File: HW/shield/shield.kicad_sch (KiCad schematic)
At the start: 28 parts

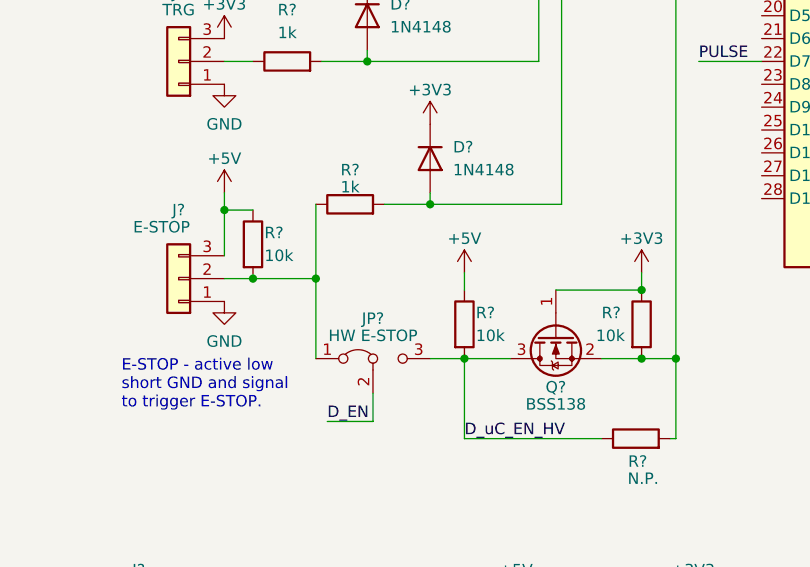
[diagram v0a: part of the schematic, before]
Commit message: added note about e-stop
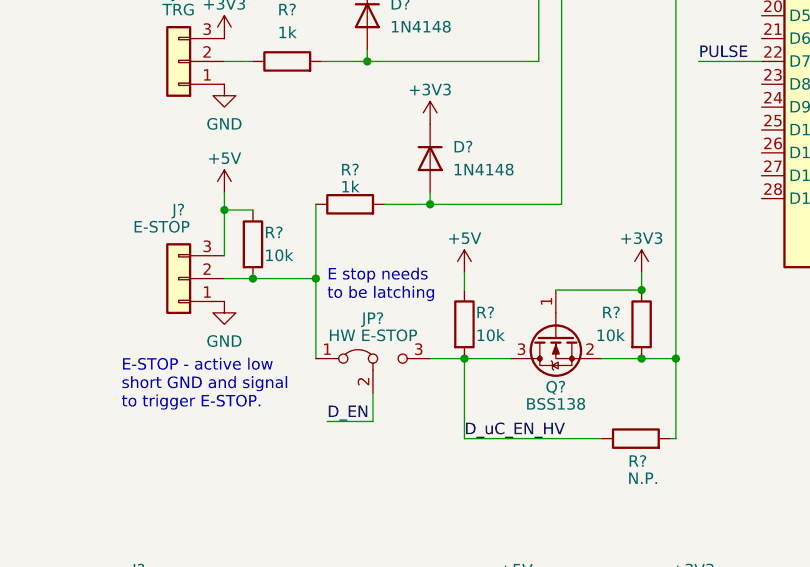
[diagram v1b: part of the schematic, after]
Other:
- note added: "E stop needs to be latching"
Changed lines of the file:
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@@
+    (effects (font (size 1.27 1.27)) (justify left bottom))
+  )
+  (text "E stop needs\nto be latching" (at 80.01 126.365 0)
     (effects (font (size 1.27 1.27)) (justify left bottom))
   )

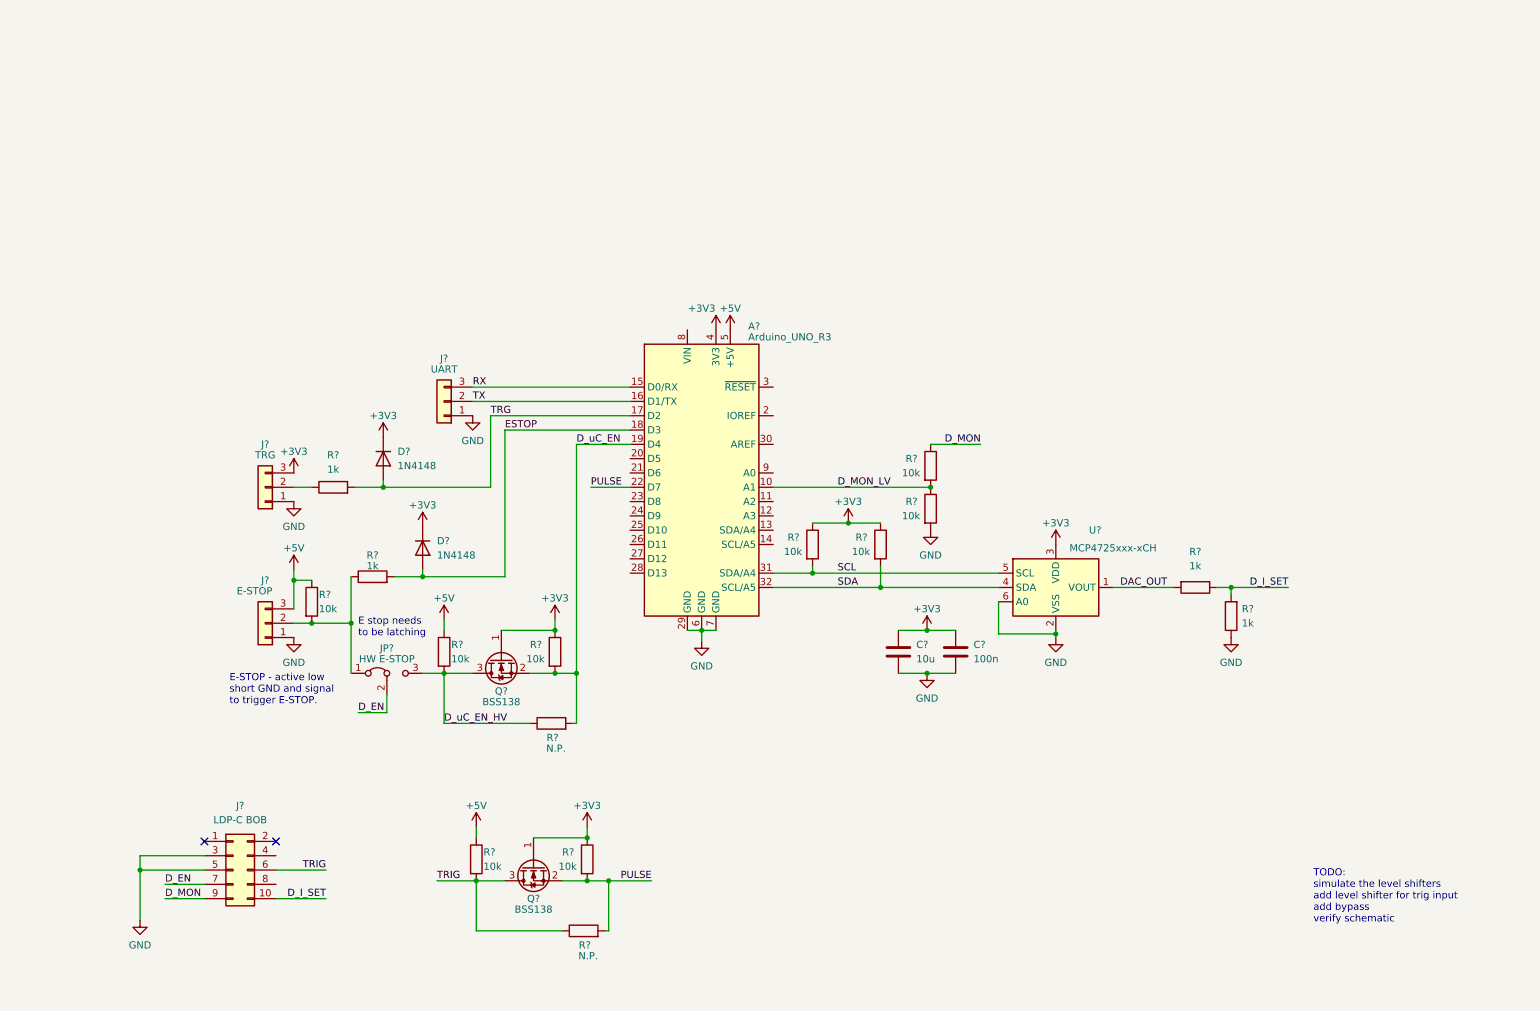
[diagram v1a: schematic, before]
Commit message: added simulation and started woking on photodiode amp
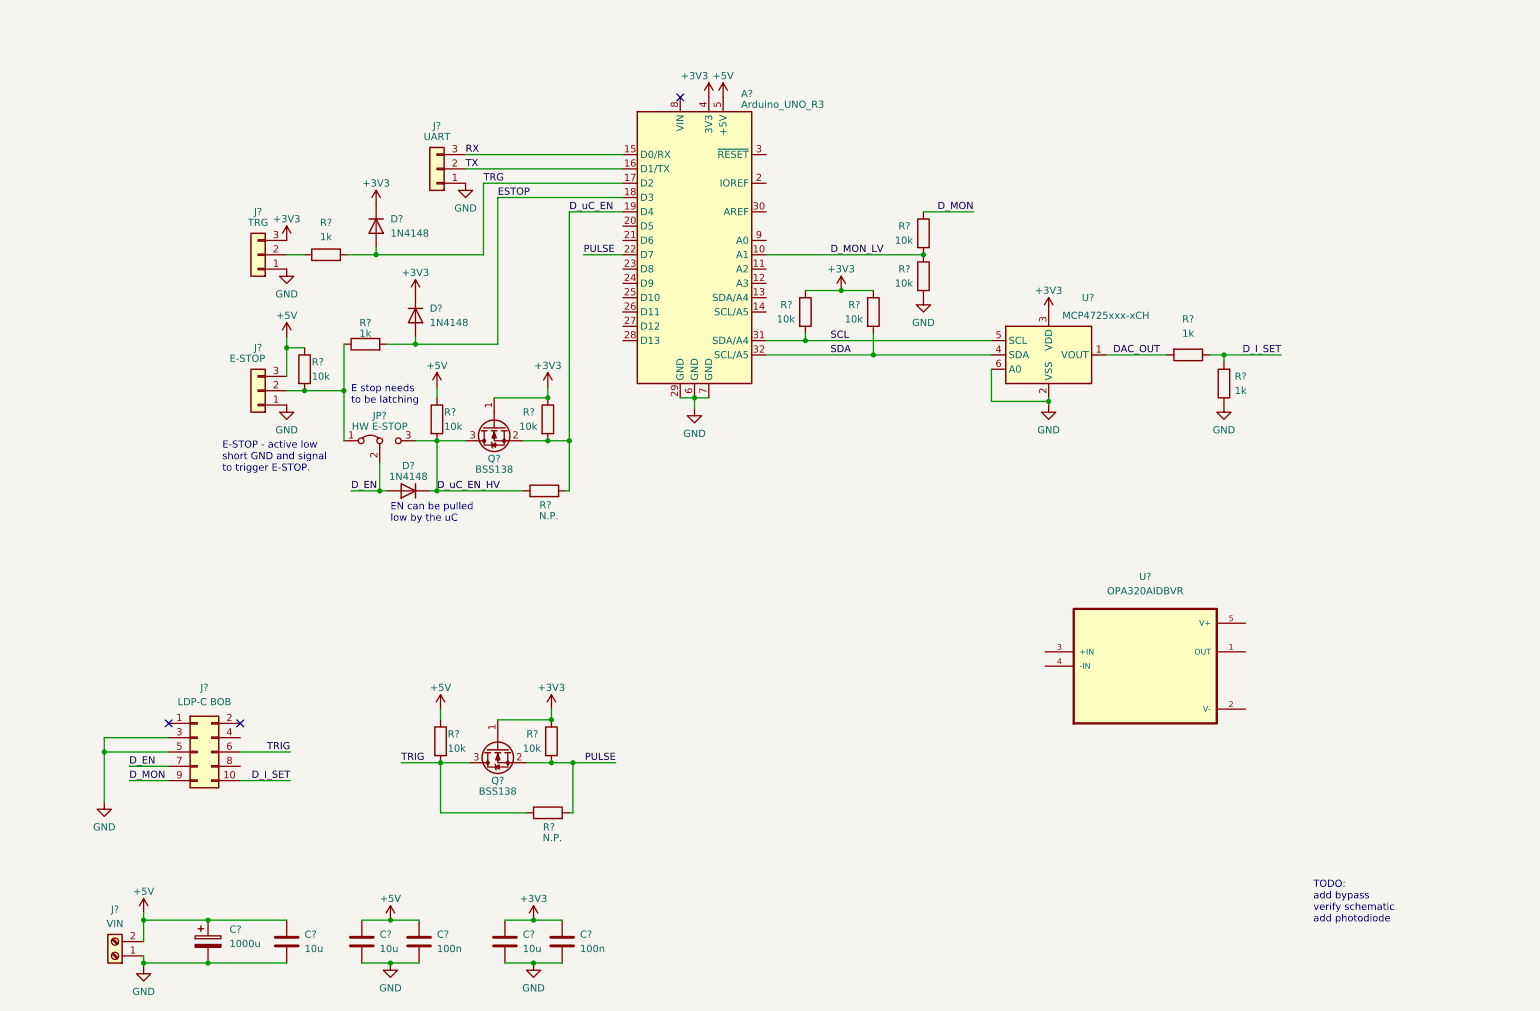
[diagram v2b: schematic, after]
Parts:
- added C?: 100n, symbol Device:C
- added C? (x2): 10u, symbol Device:C
- added C?: 1000u, symbol Device:C_Polarized
- added D?: 1N4148, symbol Device:D
- added J?: VIN, symbol Connector:Screw_Terminal_01x02
- added U?: OPA320AIDBVR, SOT95P280X145-5N, symbol OPA320AIDBVR:OPA320AIDBVR
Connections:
- net +5V: now also C?.1, C?.1, C?.1, C?.1, J?.2 (Pin_2)
- net D_EN: now also D?.2 (A)
- net D_uC_EN_HV: now also D?.1 (K)
- net GND: now also C?.2, C?.2, C?.2, C?.2, J?.1 (Pin_1)
- no-connect marks 2 -> 3
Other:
- note added: "EN can be pulled low by the uC"
- note added: "TODO: add bypass verify schematic add photodiode"
- note removed: "TODO: simulate the level shifters add level shifter for trig input add bypass verify schematic"
- moved on the sheet: A?, C?, D?, J?, JP?, Q?, R?, U?

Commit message: finished schematic
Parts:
- removed U?: OPA320AIDBVR, SOT95P280X145-5N, symbol OPA320AIDBVR:OPA320AIDBVR
- added C?: 10p, symbol Device:C
- added C? (x2): 100n, symbol Device:C
- added C?: 10u, symbol Device:C
- added D?: SFH 213, symbol Device:D_Photo
- added H? (x2): MountingHole, symbol Mechanical:MountingHole
- added J?: BREAK, symbol Connector_Generic:Conn_02x03_Odd_Even
- added J?: IO, symbol Connector:Screw_Terminal_01x06
- added Q? (x4): BSS138, Package_TO_SOT_SMD:SOT-23, symbol Transistor_FET:BSS138
- added R? (x4): N.P., symbol Device:R
- added R? (x12): 10k, symbol Device:R
- added R? (x2): 100, symbol Device:R
- added R?: 50, symbol Device:R
- added U? (x3): MCP6477-E, Package_SO:MSOP-8_3x3mm_P0.65mm, symbol Amplifier_Operational:MCP6L02x-xMS
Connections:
- net +3V3: now also Q?.1 (G), Q?.1 (G), Q?.1 (G), Q?.1 (G), R?.1, R?.1, R?.1, R?.1
- net +5V: now also C?.1, C?.1, J?.1 (Pin_1), J?.2 (Pin_2), J?.6 (Pin_6), R?.1, R?.1, R?.1, R?.1, R?.2, U?.8 (V+)
- net GND: now also C?.1, C?.2, C?.2, D?.2 (A), J?.1 (Pin_1), J?.5 (Pin_5), J?.6 (Pin_6), R?.2, U?.4 (V-), U?.5 (+)
- net IO1: now reaches A?.23 (D8)
- net IO1: now also Q?.2 (S), R?.2, R?.2
- net IO2: now reaches A?.24 (D9)
- net IO2: now also Q?.2 (S), R?.2, R?.2
- net IO3: now reaches A?.25 (D10)
- net IO3: now also Q?.2 (S), R?.2, R?.2
- net IO4: now reaches A?.26 (D11)
- net IO4: now also Q?.2 (S), R?.2, R?.2
- net D_VOUT: now reaches A?.9 (A0)
- net D_VOUT: now also J?.3 (Pin_3), J?.4 (Pin_4), R?.1
- new net: C?.1, D?.1 (K), R?.2, U?.2 (-)
- new net: C?.2, R?.1, R?.2, U?.1
- new net: R?.1, R?.2 (x3)
- new net: U?.6 (-), U?.7
- new net GUARD: C?.2, R?.1, R?.1, U?.3 (+)
- new net HV_IO1: J?.5 (Pin_5), Q?.3 (D), R?.1, R?.2
- new net HV_IO2: J?.4 (Pin_4), Q?.3 (D), R?.1, R?.2
- new net HV_IO3: J?.3 (Pin_3), Q?.3 (D), R?.1, R?.2
- new net HV_IO4: J?.2 (Pin_2), Q?.3 (D), R?.1, R?.2
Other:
- note added: "N.P."
- note added: "https://www.ti.com/lit/ug/tidu535/tidu535.pdf"
- moved on the sheet: A?, C?, D?, J?, JP?, Q?, R?, U?

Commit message: changed op amp added simulation of photodiode
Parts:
- U? (x3): value MCP6477-E -> OPA2727
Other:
- note added: "TODO: verify schematic"
- note removed: "TODO: add bypass verify schematic add photodiode"
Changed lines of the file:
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@@
     (stroke (width 0) (type default) (color 0 0 0 0))
   )
-  (text "TODO:\nadd bypass\nverify schematic\nadd photodiode" (at 249.555 177.165 0)
+  (text "TODO:\nverify schematic" (at 249.555 177.165 0)
     (effects (font (size 1.27 1.27)) (justify left bottom))
   )
@@
   (symbol (lib_id "Amplifier_Operational:MCP6L02x-xMS") (at 176.53 132.715 0) (unit 1)
     (in_bom yes) (on_board yes) (fields_autoplaced)
-    (property "Reference" "U?" (id 0) (at 176.53 122.555 0))
-    (property "Value" "MCP6477-E" (id 1) (at 176.53 125.095 0))
+    (property "Reference" "U?" (id 0) (at 176.53 121.92 0))
+    (property "Value" "OPA2727" (id 1) (at 176.53 124.46 0))
     (property "Footprint" "Package_SO:MSOP-8_3x3mm_P0.65mm" (id 2) (at 179.07 132.715 0)
       (effects (font (size 1.27 1.27)) hide)
@@
   )
   (symbol (lib_id "Connector_Generic:Conn_02x03_Odd_Even") (at 226.695 132.715 0) (unit 1)
-    (in_bom yes) (on_board yes) (fields_autoplaced)
-    (property "Reference" "J?" (id 0) (at 227.965 123.825 0))
-    (property "Value" "BREAK" (id 1) (at 227.965 126.365 0))
+    (in_bom yes) (on_board yes)
+    (property "Reference" "J?" (id 0) (at 224.79 127 0))
+    (property "Value" "BREAK" (id 1) (at 224.79 137.795 0))
     (property "Footprint" "" (id 2) (at 226.695 132.715 0)
       (effects (font (size 1.27 1.27)) hide)
@@
     (in_bom yes) (on_board yes) (fields_autoplaced)
     (property "Reference" "U?" (id 0) (at 200.025 107.95 0))
-    (property "Value" "MCP6477-E" (id 1) (at 200.025 110.49 0))
+    (property "Value" "OPA2727" (id 1) (at 200.025 110.49 0))
     (property "Footprint" "Package_SO:MSOP-8_3x3mm_P0.65mm" (id 2) (at 202.565 118.11 0)
       (effects (font (size 1.27 1.27)) hide)
@@
       (effects (font (size 1.27 1.27)) (justify left))
     )
-    (property "Value" "MCP6477-E" (id 1) (at 194.945 140.97 0)
+    (property "Value" "OPA2727" (id 1) (at 194.945 140.97 0)
       (effects (font (size 1.27 1.27)) (justify left))
     )
@@
     )
     (path "/3d49a01e-4cc6-4978-a1ca-5d017152c016"
-      (reference "U?") (unit 1) (value "MCP6477-E") (footprint "Package_SO:MSOP-8_3x3mm_P0.65mm")
+      (reference "U?") (unit 1) (value "OPA2727") (footprint "Package_SO:MSOP-8_3x3mm_P0.65mm")
     )
     (path "/43bf58bc-9b32-48f4-b206-bc9c56cfef4b"
-      (reference "U?") (unit 2) (value "MCP6477-E") (footprint "Package_SO:MSOP-8_3x3mm_P0.65mm")
+      (reference "U?") (unit 2) (value "OPA2727") (footprint "Package_SO:MSOP-8_3x3mm_P0.65mm")
     )
     (path "/7c60fdb6-dd36-4929-9a3d-75eb61fe5020"
-      (reference "U?") (unit 3) (value "MCP6477-E") (footprint "Package_SO:MSOP-8_3x3mm_P0.65mm")
-    )
-  )
+      (reference "U?") (unit 3) (value "OPA2727") (footprint "Package_SO:MSOP-8_3x3mm_P0.65mm")
+    )
+  )

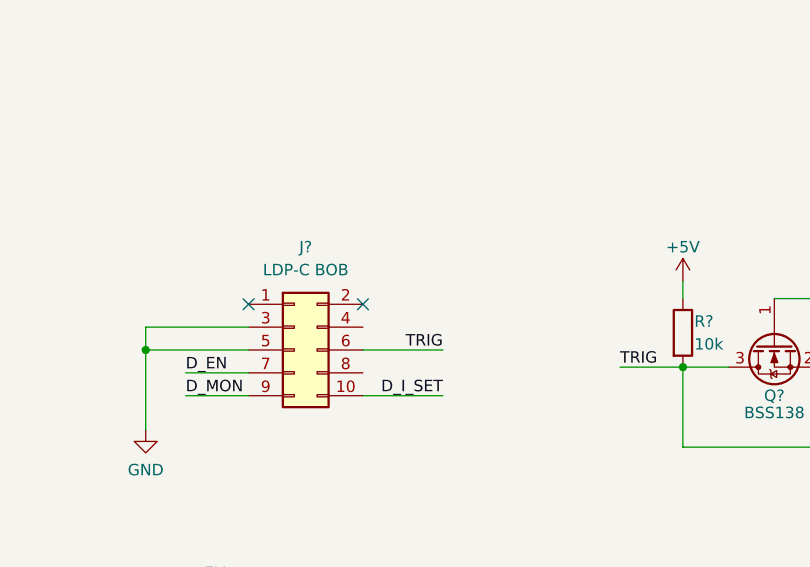
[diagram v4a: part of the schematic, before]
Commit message: small schematic changes
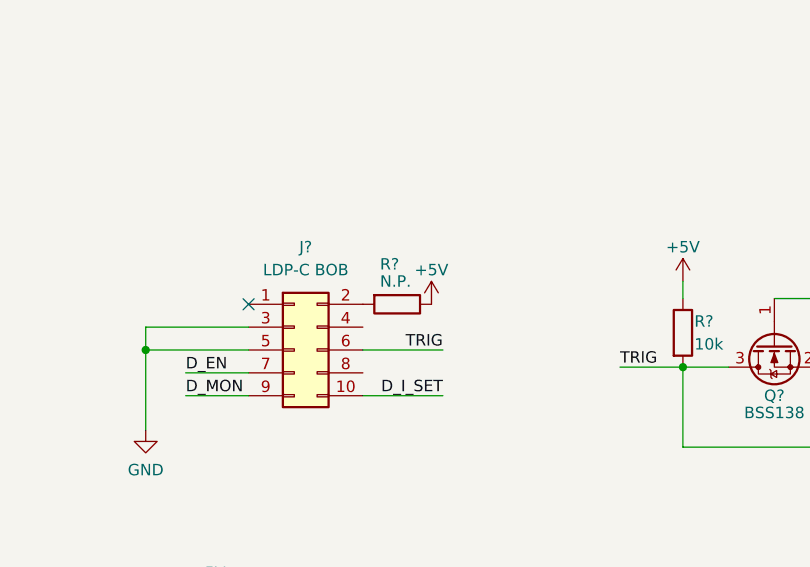
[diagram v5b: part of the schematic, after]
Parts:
- added R?: N.P., symbol Device:R
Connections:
- net +5V: now also R?.1
- net at J?.2 (Pin_2): now also R?.2
- no-connect marks 3 -> 2
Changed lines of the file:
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@@
   (no_connect (at 99.695 20.32))
   (no_connect (at 44.45 132.08))
-  (no_connect (at 57.15 132.08))
   (wire (pts (xy 51.435 167.005) (xy 65.405 167.005))
     (stroke (width 0) (type default) (color 0 0 0 0))
@@
     (pin "8")
   )
+  (symbol (lib_id "power:+5V") (at 64.77 132.08 0) (unit 1)
+    (in_bom yes) (on_board yes)
+    (property "Reference" "#PWR?" (id 0) (at 64.77 135.89 0)
+      (effects (font (size 1.27 1.27)) hide)
+    )
+    (property "Value" "+5V" (id 1) (at 64.77 128.27 0))
+    (property "Footprint" "" (id 2) (at 64.77 132.08 0)
+      (effects (font (size 1.27 1.27)) hide)
+    )
+    (property "Datasheet" "" (id 3) (at 64.77 132.08 0)
+      (effects (font (size 1.27 1.27)) hide)
+    )
+    (pin "1")
+  )
   (symbol (lib_id "power:GND") (at 29.845 74.93 0) (unit 1)
     (in_bom yes) (on_board yes) (fields_autoplaced)
@@
     )
     (property "Datasheet" "~" (id 3) (at 269.875 40.64 0)
+      (effects (font (size 1.27 1.27)) hide)
+    )
+    (pin "1")
+    (pin "2")
+  )
+  (symbol (lib_id "Device:R") (at 60.96 132.08 270) (unit 1)
+    (in_bom yes) (on_board yes)
+    (property "Reference" "R?" (id 0) (at 59.055 127.635 90)
+      (effects (font (size 1.27 1.27)) (justify left))
+    )
+    (property "Value" "N.P." (id 1) (at 59.055 129.54 90)
+      (effects (font (size 1.27 1.27)) (justify left))
+    )
+    (property "Footprint" "" (id 2) (at 60.96 130.302 90)
+      (effects (font (size 1.27 1.27)) hide)
+    )
+    (property "Datasheet" "~" (id 3) (at 60.96 132.08 0)
       (effects (font (size 1.27 1.27)) hide)
     )
@@
       (reference "#PWR?") (unit 1) (value "GND") (footprint "")
     )
+    (path "/4498f9de-1b76-432d-bf96-a7a8be0bccdd"
+      (reference "#PWR?") (unit 1) (value "+5V") (footprint "")
+    )
     (path "/460fdbc3-5a62-4e7e-a3a7-923a5b1975d6"
       (reference "#PWR?") (unit 1) (value "GND") (footprint "")
@@
       (reference "R?") (unit 1) (value "10k") (footprint "")
     )
+    (path "/b3abeee2-cb51-4396-a413-9eb16f44d456"
+      (reference "R?") (unit 1) (value "N.P.") (footprint "")
+    )
     (path "/c029db6a-259d-4adf-a8bd-35c698951b05"
